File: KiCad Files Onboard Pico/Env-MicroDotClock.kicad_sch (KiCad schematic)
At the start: 59 parts, among them IC1 IS31FL3730-QFLS2-TR, IC2 IS31FL3730-QFLS2-TR, IC3 IS31FL3730-QFLS2-TR, IC4 IS31FL3730-QFLS2-TR, J1 1mm 1x3, M1 Dip-14 Socket, M2 Dip-14 Socket, M3 Dip-14 Socket, M4 Dip-14 Socket, M5 Dip-14 Socket, M6 Dip-14 Socket, M7 Dip-14 Socket, M8 Dip-14 Socket, Q1 2SC1815, SW1 MX Keyboard Switch, SW2 MX Keyboard Switch, SW3 MX Keyboard Switch, SW4 MX Keyboard Switch, SW5 MX Keyboard Switch, U1 Si7021-A20, U3 DS3231M

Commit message: added a text note
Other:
- note added: "THE IS31FL3730S NEED TO RUN OFF 5V, LEVEL SHIFT THE GPIO"

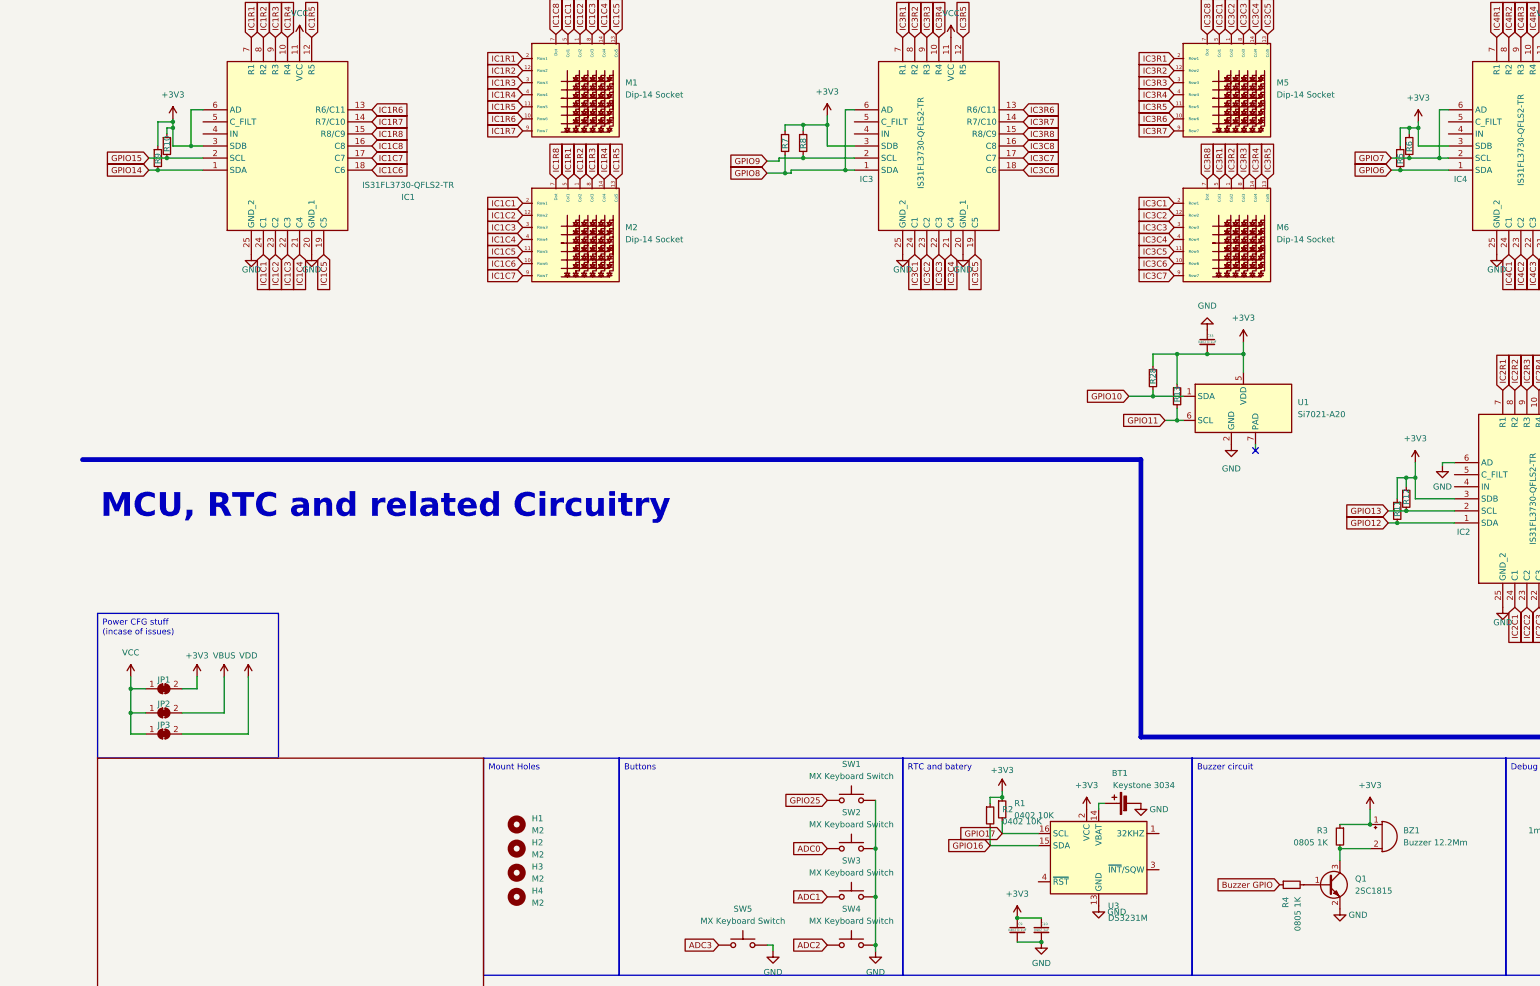
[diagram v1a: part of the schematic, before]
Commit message: Moved all ICs to one i2c bus, removed SI7021, added i2c level shifters.
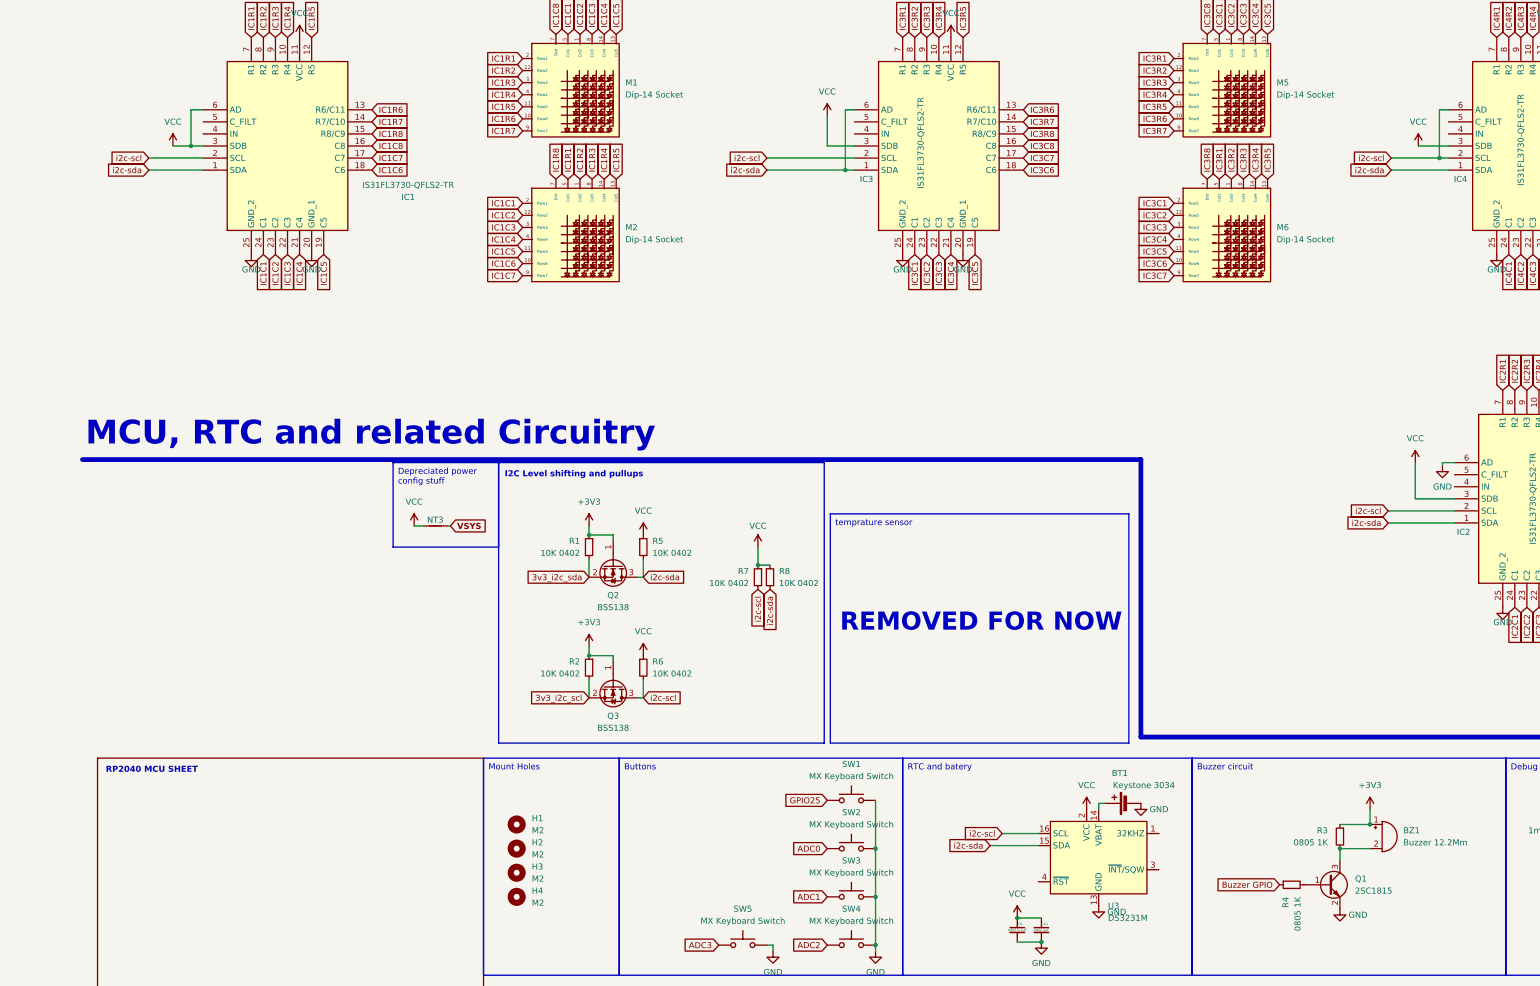
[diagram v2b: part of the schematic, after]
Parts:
- removed C33: 0402 0.1uF, Capacitor_SMD:C_0402_1005Metric, symbol Device:C_Small
- removed JP1: bridge, Jumper:SolderJumper-2_P1.3mm_Bridged_RoundedPad1.0x1.5mm, symbol Jumper:SolderJumper_2_Bridged
- removed JP2, JP3: bridge, Jumper:SolderJumper-2_P1.3mm_Open_RoundedPad1.0x1.5mm, symbol Jumper:SolderJumper_2_Bridged
- removed R10, R11, R12, R13, R28, R9: 0402 10K, Resistor_SMD:R_0402_1005Metric, symbol Device:R_Small
- removed U1: Si7021-A20, Package_DFN_QFN:DFN-6-1EP_3x3mm_P1mm_EP1.5x2.4mm, symbol Sensor_Humidity:Si7021-A20
- added NT3: NetTie_2, NetTie:NetTie-2_THT_Pad0.3mm, symbol Device:NetTie_2
- added Q2, Q3: BSS138, Package_TO_SOT_SMD:SOT-23, symbol Transistor_FET:BSS138
- R1, R2, R5, R6, R7, R8: value 0402 10K -> 10K 0402
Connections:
- net GPIO14 is gone; now on net i2c-sda: IC1.1 (SDA)
- net GPIO15 is gone; now on net i2c-scl: IC1.2 (SCL)
- net GPIO6 is gone; now on net i2c-sda: IC4.1 (SDA), R5.2
- net GPIO7 is gone; now on net i2c-scl: IC4.2 (SCL), IC4.6 (AD), R6.2
- net +3V3: now also Q2.1 (G), Q3.1 (G); no longer C10.1, C9.1, IC1.3 (SDB), IC1.6 (AD), IC2.3 (SDB), IC3.3 (SDB), IC4.3 (SDB), R5.1, R6.1, R7.1, R8.1, U3.2 (VCC)
- net VCC: now also C10.1, C9.1, IC1.3 (SDB), IC1.6 (AD), IC2.3 (SDB), IC3.3 (SDB), IC4.3 (SDB), R5.1, R6.1, R7.1, R8.1, U3.2 (VCC), NT3.1
- net GPIO12 renamed i2c-sda
- net i2c-sda: now also IC3.1 (SDA), IC3.6 (AD), R8.2, U3.15 (SDA), Q2.3 (D)
- net GPIO13 renamed i2c-scl
- net i2c-scl: now also IC3.2 (SCL), R7.2, U3.16 (SCL), Q3.3 (D)
- net GPIO16 renamed 3v3_i2c_scl
- net 3v3_i2c_scl: now also Q3.2 (S); no longer U3.15 (SDA)
- net GPIO17 renamed 3v3_i2c_sda
- net 3v3_i2c_sda: now also Q2.2 (S); no longer U3.16 (SCL)
- removed net GPIO8: IC3.1 (SDA), IC3.6 (AD), R7.2
- removed net GPIO9: IC3.2 (SCL), R8.2
- new net VSYS: NT3.2
- no-connect marks 1 -> 0
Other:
- note added: "I2C Level shifting and pullups"
- note added: "REMOVED FOR NOW"
- note added: "RP2040 MCU SHEET"

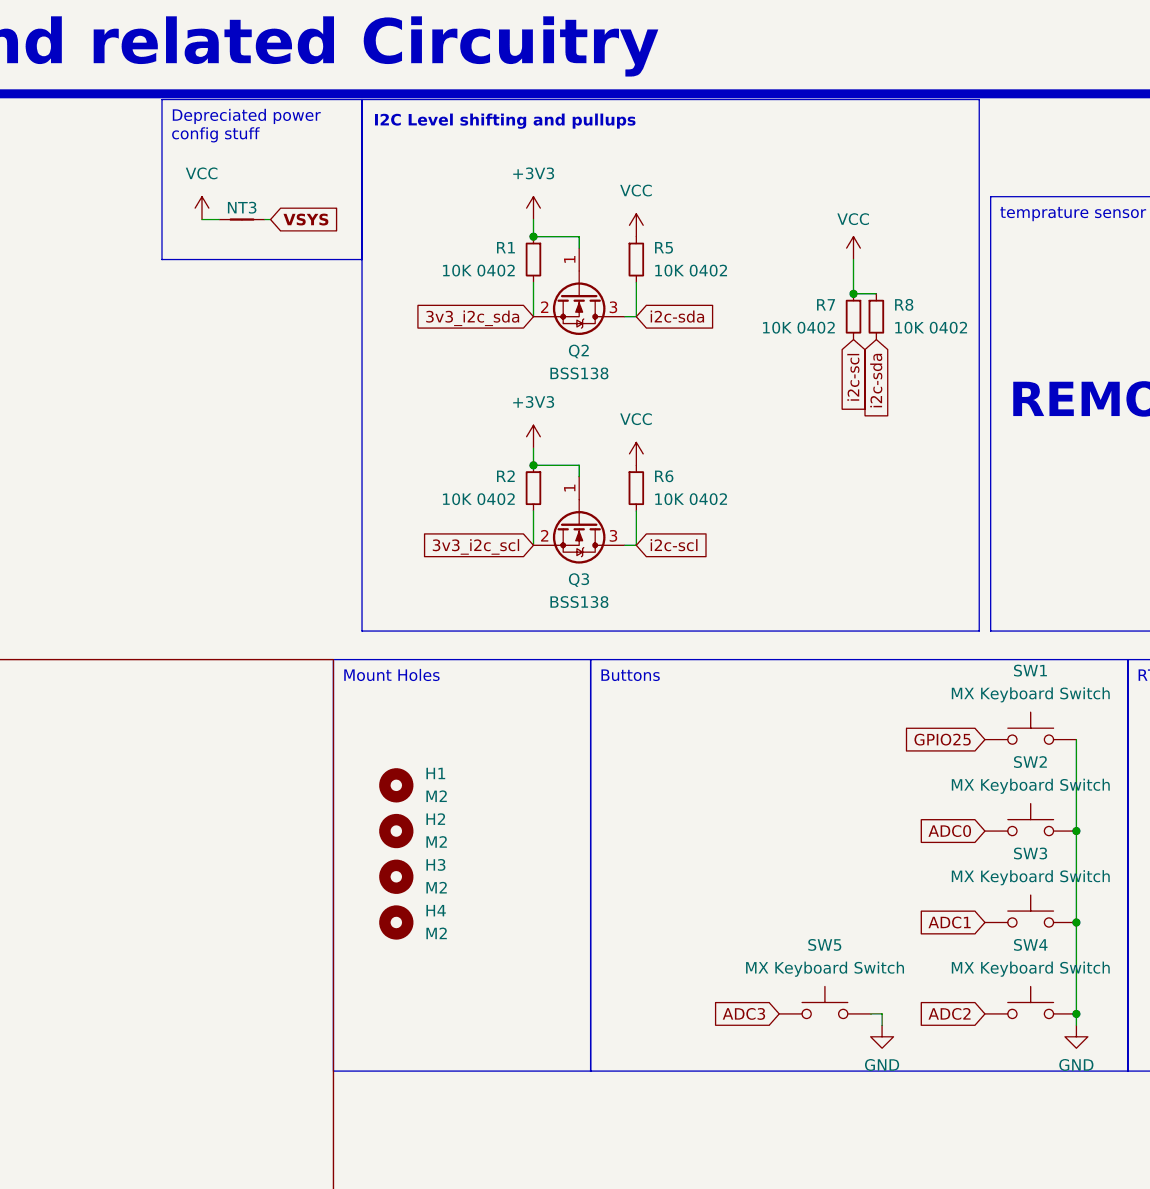
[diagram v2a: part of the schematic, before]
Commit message: Fixed issues with I2C, added I2C shifter
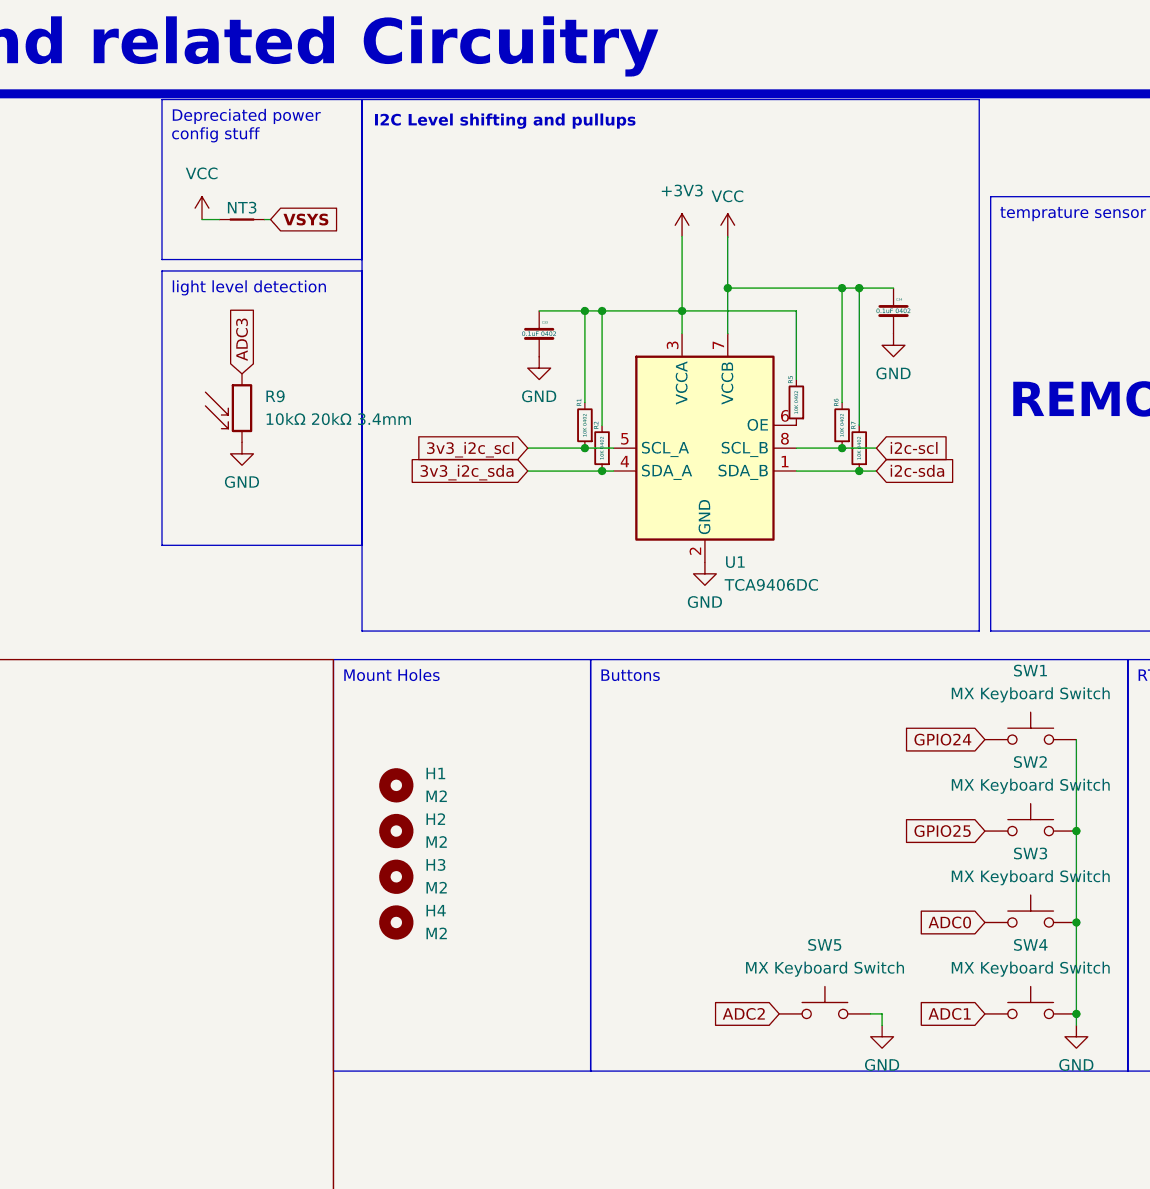
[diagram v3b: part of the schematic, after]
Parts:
- removed Q2, Q3: BSS138, Package_TO_SOT_SMD:SOT-23, symbol Transistor_FET:BSS138
- removed R8: 10K 0402, Resistor_SMD:R_0402_1005Metric, symbol Device:R_Small
- added C33, C34: 0.1uF 0402, Capacitor_SMD:C_0402_1005Metric, symbol Device:C_Small
- added R9: 10kΩ 20kΩ 3.4mm, OptoDevice:R_LDR_5.1x4.3mm_P3.4mm_Vertical, symbol Device:R_Photo
- added U1: TCA9406DC, Package_SO:VSSOP-8_2.3x2mm_P0.5mm, symbol Interface:TCA9406DC
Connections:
- net +3V3: now also R1.2, R2.2, R5.2, C33.1, U1.3 (VCCA); no longer R1.1, R2.1
- net 3v3_i2c_scl: now also R1.1, U1.5 (SCL_A); no longer R2.2
- net 3v3_i2c_sda: now also R2.1, U1.4 (SDA_A); no longer R1.2
- net ADC0: now also SW3.1; no longer SW2.1
- net ADC1: now also SW4.1; no longer SW3.1
- net ADC2: now also SW5.1; no longer SW4.1
- net ADC3: now also R9.1; no longer SW5.1
- net GND: now also C33.2, C34.2, R9.2, U1.2 (GND)
- net GPIO25: now also SW2.1; no longer SW1.1
- net VCC: now also R6.2, R7.2, C34.1, U1.7 (VCCB); no longer R5.1, R6.1, R7.1
- net i2c-scl: now also R6.1, U1.8 (SCL_B); no longer R6.2, R7.2
- net i2c-sda: now also R7.1, U1.1 (SDA_B); no longer R5.2
- new net: R5.1, U1.6 (OE)
- new net GPIO24: SW1.1

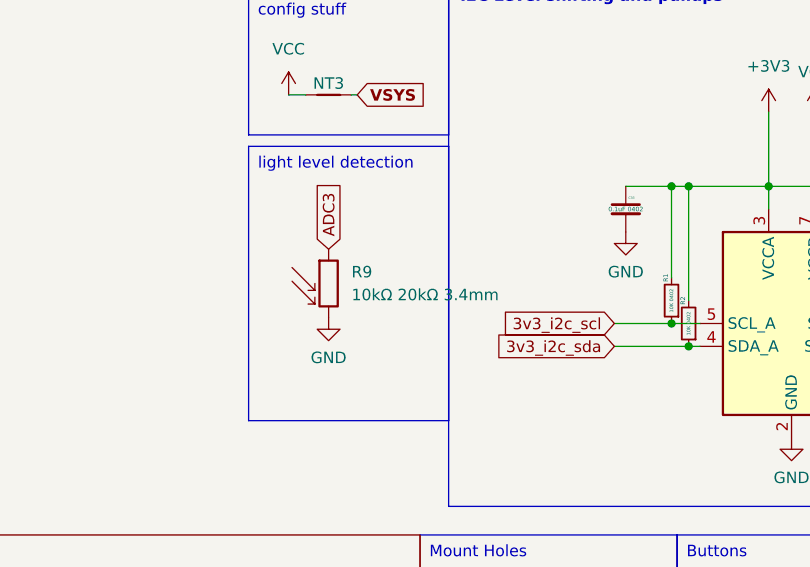
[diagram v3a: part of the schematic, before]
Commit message: corrected couple missing connections
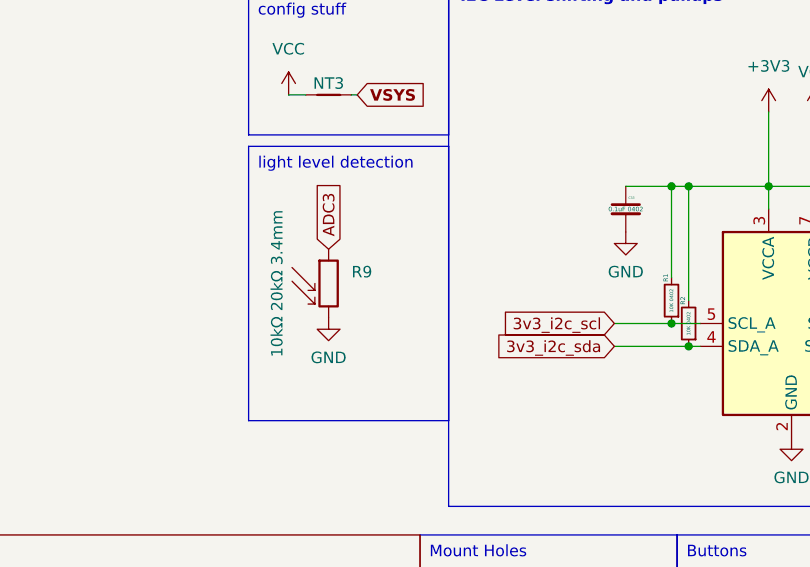
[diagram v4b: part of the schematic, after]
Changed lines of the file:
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@@
 		(on_board yes)
 		(dnp no)
-		(fields_autoplaced yes)
 		(property "Reference" "R9"
 			(at 88.9 172.7199 0)
@@
 		)
 		(property "Value" "10kΩ 20kΩ 3.4mm"
-			(at 88.9 175.2599 0)
+			(at 80.645 173.99 90)
 			(effects
 				(font
 					(size 1.27 1.27)
 				)
-				(justify left)
 			)
 		)

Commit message: forgot to fill zone
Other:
- note removed: "THE IS31FL3730S NEED TO RUN OFF 5V, LEVEL SHIFT THE GPIO"
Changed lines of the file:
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@@
-		)
-	)
-	(text "THE IS31FL3730S NEED TO RUN OFF 5V, LEVEL SHIFT THE GPIO"
-		(exclude_from_sim no)
-		(at 210.058 1.524 0)
-		(effects
-			(font
-				(size 7.62 7.62)
-				(thickness 1.524)
-				(bold yes)
-			)
 		)
 	)

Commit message: removed sockets, added level shifter IC, changed RTC to smaller package, re-did entire board to be more tidy.
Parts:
- removed C1, C3, C5, C7: 0402 0.1uF, Capacitor_SMD:C_0402_1005Metric, symbol Device:C_Small
- removed C11, C12, C13, C14: 0402 10uF, Capacitor_SMD:C_0402_1005Metric, symbol Device:C_Small
- removed C2, C4, C6, C8: 0402 1uF, Capacitor_SMD:C_0402_1005Metric, symbol Device:C_Small
- removed IC1, IC2, IC3, IC4: IS31FL3730-QFLS2-TR, Package_DFN_QFN:QFN-24-1EP_4x4mm_P0.5mm_EP2.6x2.6mm_ThermalVias, symbol IS31FL3730-QFLS2-TR:IS31FL3730-QFLS2-TR
- removed M1, M2, M3, M4, M5, M6, M7, M8: Dip-14 Socket, Package_DIP:DIP-14_W7.62mm_Socket, symbol ltp-305g:LTP-305G
- removed U3: DS3231M, Package_SO:SOIC-16W_7.5x10.3mm_P1.27mm, symbol Timer_RTC:DS3231M
- added BT2: Keystone 3034, Battery:BatteryHolder_Keystone_3034_1x20mm, symbol Device:Battery_Cell
- added U3: DS3231MZ, Package_SO:SOIC-8_3.9x4.9mm_P1.27mm, symbol Timer_RTC:DS3231MZ
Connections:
- net GND: now also BT2.2 (-), U3.5 (GND)
- net VCC: now also U3.6 (VBAT)
- net at BT1.1 (+): now also BT2.1 (+), U3.2 (VCC)
- net i2c-scl renamed I2C_SCL_5V0
- net I2C_SCL_5V0: now also U3.8 (SCL)
- net i2c-sda renamed I2C_SDA_5V0
- net I2C_SDA_5V0: now also U3.7 (SDA)
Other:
- added sheet IS31FL3731 - 01 (IS31FL3731 - 01.kicad_sch)
- added sheet IS31FL3731 - 02 (IS31FL3731 - 02.kicad_sch)
- added sheet IS31FL3731 - 03 (IS31FL3731 - 03.kicad_sch)
- added sheet IS31FL3731 - 04 (IS31FL3731 - 04.kicad_sch)
